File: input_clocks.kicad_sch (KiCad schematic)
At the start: 90 parts, among them J201 REFIN, J202 REFIN_DIRECT_P, J203 REFIN_DIRECT_N, J208 VTUNE, Q501 BFP181, Q502 BFP181, T201 TC2-1T+, U203 TSV914, U204 74LVC1G66, U501 LT1461AxS8-3.3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

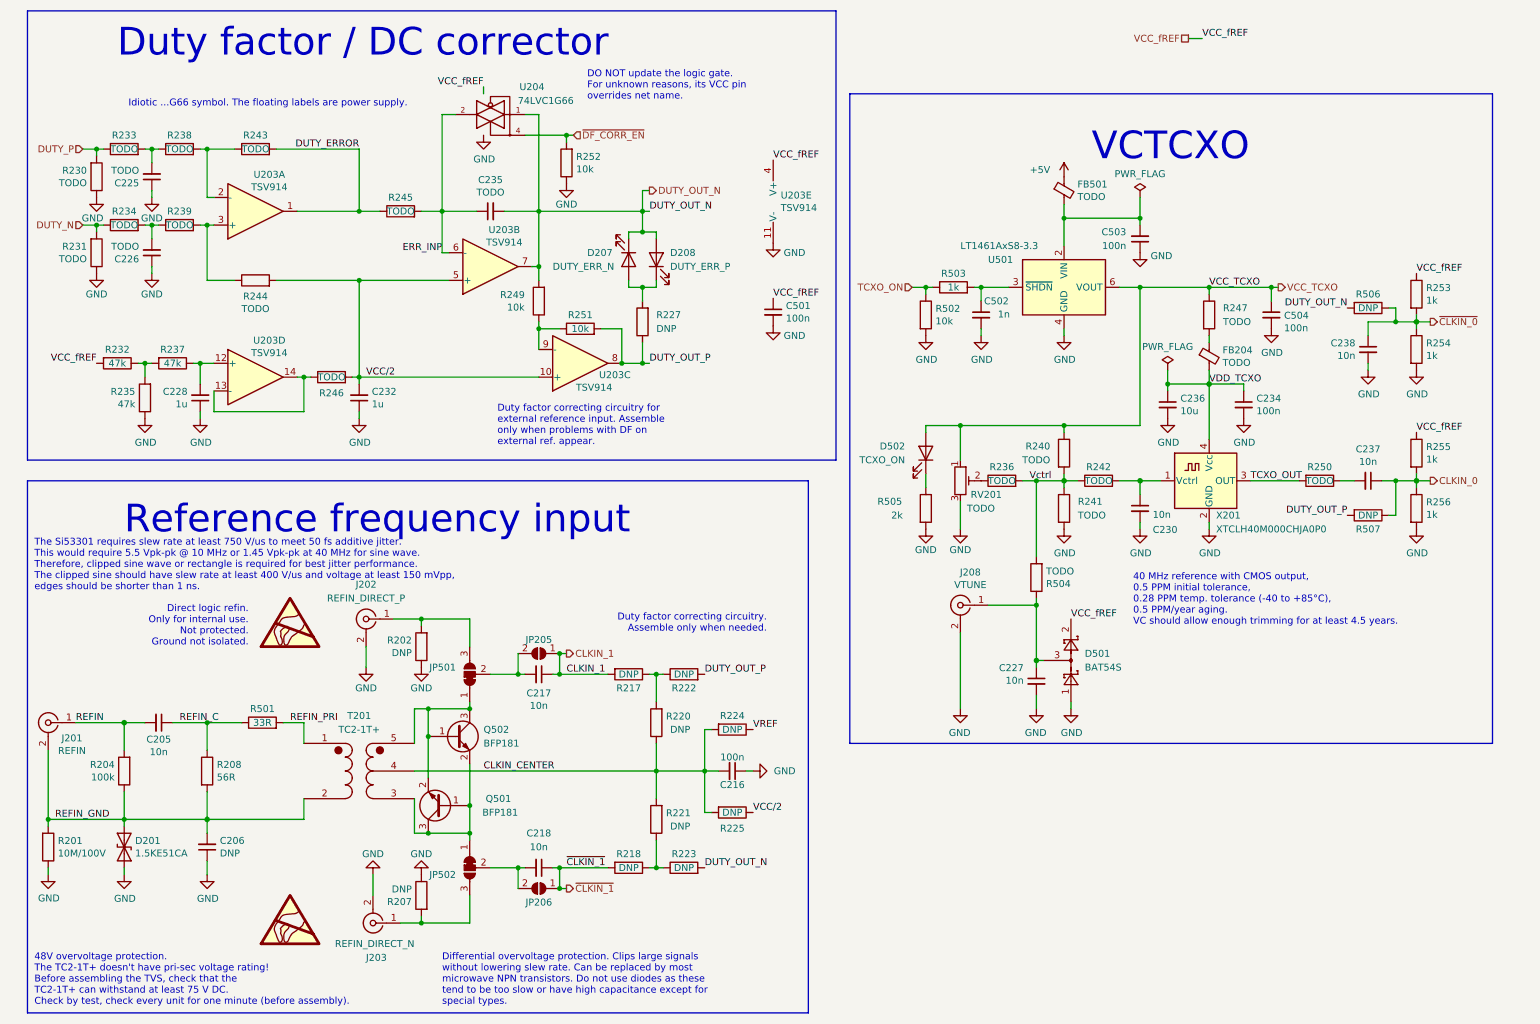
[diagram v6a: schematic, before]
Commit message: Remade and simplified AUX/EXT section.
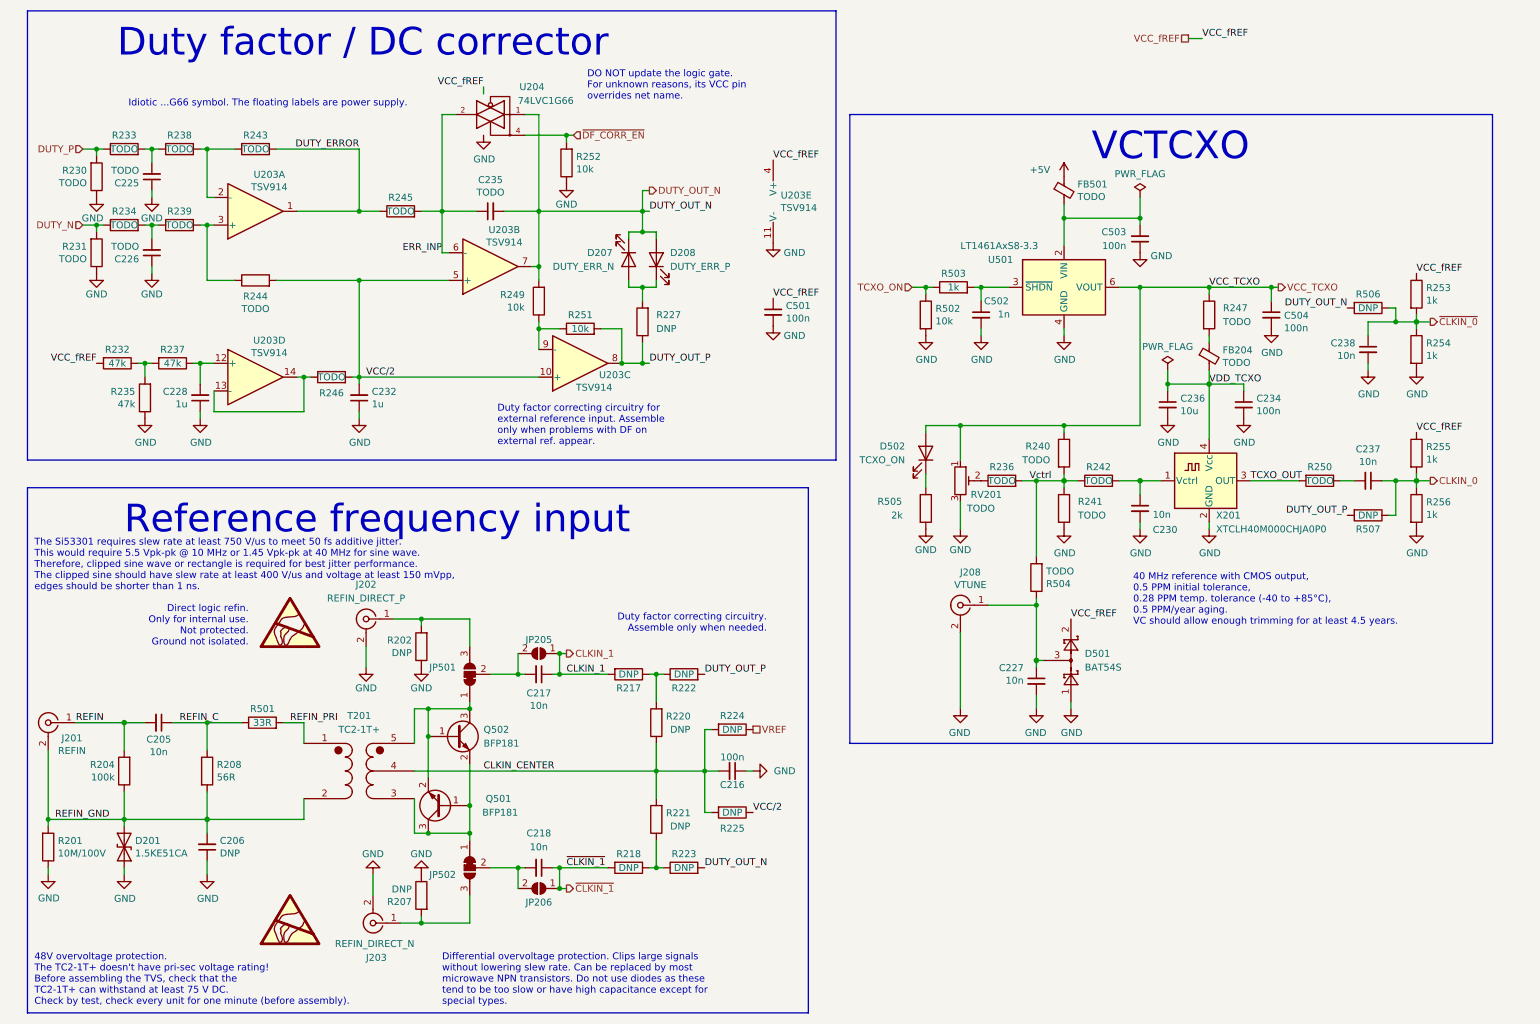
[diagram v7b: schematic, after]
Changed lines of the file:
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@@
     (stroke (width 0) (type default) (color 0 0 0 0))
   )
-  (polyline (pts (xy 156.21 196.85) (xy 156.21 99.06))
-    (stroke (width 0) (type default) (color 0 0 0 0))
-  )
-  (polyline (pts (xy 156.21 99.06) (xy 12.7 99.06))
+  (polyline (pts (xy 156.21 196.85) (xy 156.21 100.33))
+    (stroke (width 0) (type default) (color 0 0 0 0))
+  )
+  (polyline (pts (xy 156.21 100.33) (xy 12.7 100.33))
     (stroke (width 0) (type default) (color 0 0 0 0))
   )
@@
     (stroke (width 0) (type default) (color 0 0 0 0))
   )
-  (polyline (pts (xy 12.7 99.06) (xy 12.7 196.85))
+  (polyline (pts (xy 12.7 100.33) (xy 12.7 196.85))
     (stroke (width 0) (type default) (color 0 0 0 0))
   )
@@
     (stroke (width 0) (type solid) (color 0 0 0 0))
   )
-  (polyline (pts (xy 281.94 27.94) (xy 281.94 147.32))
-    (stroke (width 0) (type default) (color 0 0 0 0))
-  )
-  (polyline (pts (xy 163.83 27.94) (xy 281.94 27.94))
+  (polyline (pts (xy 281.94 31.75) (xy 281.94 147.32))
+    (stroke (width 0) (type default) (color 0 0 0 0))
+  )
+  (polyline (pts (xy 163.83 31.75) (xy 281.94 31.75))
     (stroke (width 0) (type default) (color 0 0 0 0))
   )
@@
     (stroke (width 0) (type default) (color 0 0 0 0))
   )
-  (polyline (pts (xy 163.83 27.94) (xy 163.83 147.32))
+  (polyline (pts (xy 163.83 31.75) (xy 163.83 147.32))
     (stroke (width 0) (type default) (color 0 0 0 0))
   )
@@
     (effects (font (size 1.27 1.27)) (justify left bottom))
   )
-  (label "VREF" (at 146.05 144.78 0)
-    (effects (font (size 1.27 1.27)) (justify left bottom))
-  )
   (label "TCXO_OUT" (at 237.49 99.06 0)
     (effects (font (size 1.27 1.27)) (justify left bottom))
@@
     (effects (font (size 1.27 1.27)) (justify left))
   )
+  (hierarchical_label "VREF" (shape passive) (at 146.05 144.78 0)
+    (effects (font (size 1.27 1.27)) (justify left))
+  )

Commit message: Fixes.
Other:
- title: Generator 0.0125 - 6.4 GHz (0.02 - 9.8 GHz) -> Generator 0.0125 - 6.4 GHz (or up to 20 GHz)
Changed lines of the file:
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@@
   (paper "A4")
   (title_block
-    (title "Generator 0.0125 - 6.4 GHz (0.02 - 9.8 GHz)")
-    (date "2021-11-13")
-    (rev "211113-001")
+    (title "Generator 0.0125 - 6.4 GHz (or up to 20 GHz)")
+    (date "2021-12-30")
+    (rev "211230-001")
     (company "Petr Polasek")
-    (comment 1 "001, 2021-11-13 09:38")
-    (comment 2 "TCXO / external input, LMX2572/LMX2592")
-    (comment 3 "Dual channel symmetric outputs")
+    (comment 1 "001, 2021-12-30 00:50")
+    (comment 2 "TCXO / external input")
+    (comment 3 "LMX2572 (6.4 GHz) / LMX2592 (9.8GHz) / LMX2594 (15 GHz) / LMX2595 (20 GHz)")
   )
   (junction (at 85.09 180.34) (diameter 0) (color 0 0 0 0)
